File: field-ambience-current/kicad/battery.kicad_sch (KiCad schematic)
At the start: 16 parts, among them J9 JST PH 2.0 2-pin (LiPo Batter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, Q1 DMG2305UX P-MOS SOT-23 (USB-C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, U7 MCP73831T-2ACI/OT (LiPo Charg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, U8 TPS61089RNSR (Boost LiPo→5V, 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

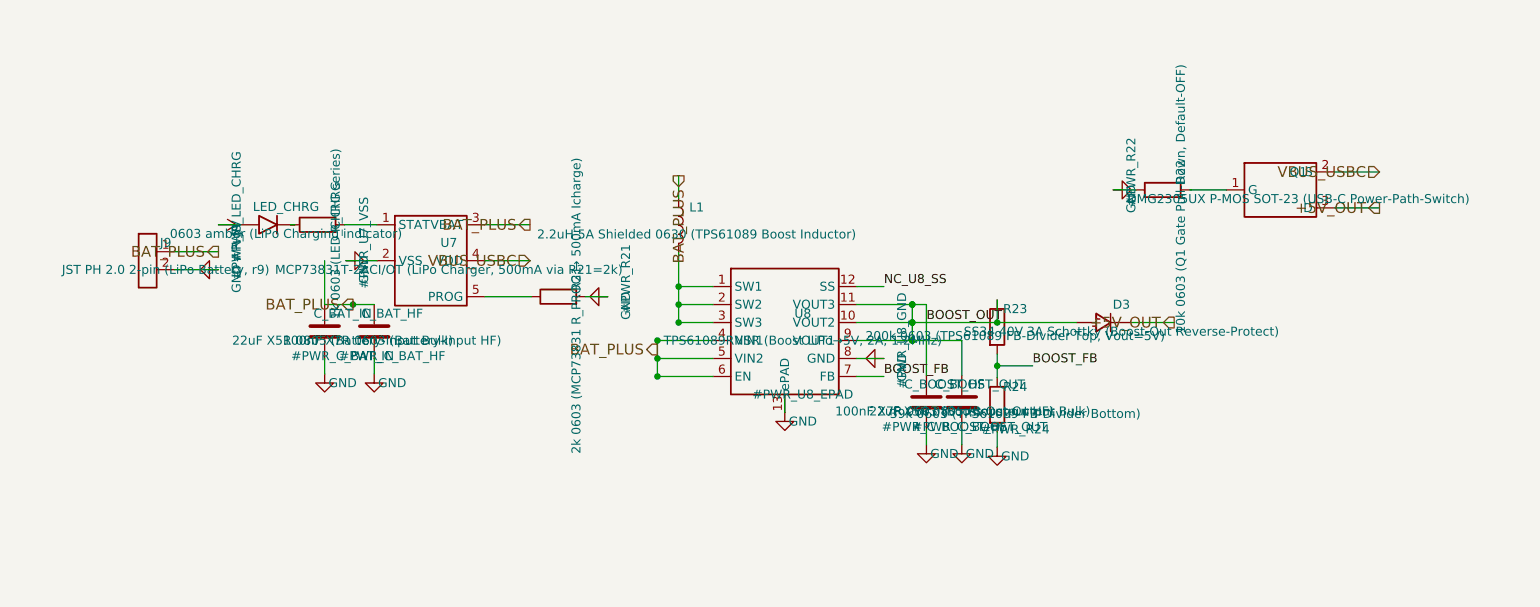
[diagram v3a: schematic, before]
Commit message: pcb(gen): r12-B11 RESOLVED — TPS61089-Refactor RNSR → RNR (JLC-soviel-wie-möglich)
User-Decision: Option 1 (JLC-Bestücken-Strategie). TPS61089RNSR (QFN-12 3×3
nicht bei LCSC verfügbar) gegen TPS61089RNR (VQFN-11 HotRod 2×2.5 + ePAD,
LCSC C165129 Extended $0.41, 2.775 Stock) getauscht.

Generator-Changes:
- _tps61089_lib_symbol() komplett neu auf 11 Pins per TI Datasheet SLVSD38C:
  FSW, VCC, FB, COMP, GND, VOUT (left); SW, BOOT, VIN, ILIM, EN (right); ePAD
- battery_sheet U8-Block komplett umverdrahtet — neuer Pinout, alle 11 Pins
  + ePAD korrekt connected
- 6 neue externe Bauteile (alle BASIC oder PREFERRED, keine Extended-Fees!):
  * C_VCC 1µF (C15849) — interne LDO-Decoupling (Datasheet >=1µF)
  * R_FSW 360k (C23146 PREF) — Fsw ~1.21 MHz (über Audio-Band wie SPEC)
  * R_ILIM 20k (C4184) — current-limit ~4A peak (matches TPS-2A-output)
  * C_BOOT 100nF (C14663) — high-side gate-driver bootstrap zwischen BOOT+SW
  * R_COMP 22k (C31850) + C_COMP 1nF (C1588) — Type-II loop-compensation

Side-Bug aufgefangen während Refactor: erste R23-pin1-Wire ging vertikal
DURCH R23+R24-Body und shortete den FB-Divider (Analyzer zeigte BOOST_FB 6 pins
statt 3 inkl. U8.6 VOUT). Fix: Label-only-Connect statt durchgehende Wire.

Analyzer-Result nach Refactor (verifiziert via kicad-skill):
- Errors: 6 (unchanged, alle pre-existing VM-001 false-positives)
- Warnings: 22 → 21
- Trust: 79.8% → 81.4%
- Critical Nets korrekt connected:
  * BAT_PLUS: 8 pins (R_BAT_DIV_TOP, J9.1, U7.3, C_BAT_IN/HF, U8.9 VIN,
    U8.7 EN, L1.1)
  * BOOST_OUT: 5 pins (U8.6 VOUT, R23.1, C_BOOST_OUT, C_BOOST_HF, D3.2 A)
  * BOOST_FB: 3 pins (U8.3 FB, R23.2, R24.1) — Divider sauber
  * U8_SW_NODE: 4 pins (U8.11 SW, L1.2, C_BOOT.2, R_FSW.1)
  * U8_BOOT_NODE: 2 pins (U8.10 BOOT, C_BOOT.1)

SPEC §2.2 + PCB_TODO r12-B11 als RESOLVED markiert. Footprint
"Package_DFN_QFN:VQFN-11-1EP_2.6x2.6mm_P0.5mm_EP0.85x1.5mm_HotRod" als String
gesetzt — die exakte KiCad-Library-Match muss im KiCad-GUI verifiziert werden
(könnte ein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
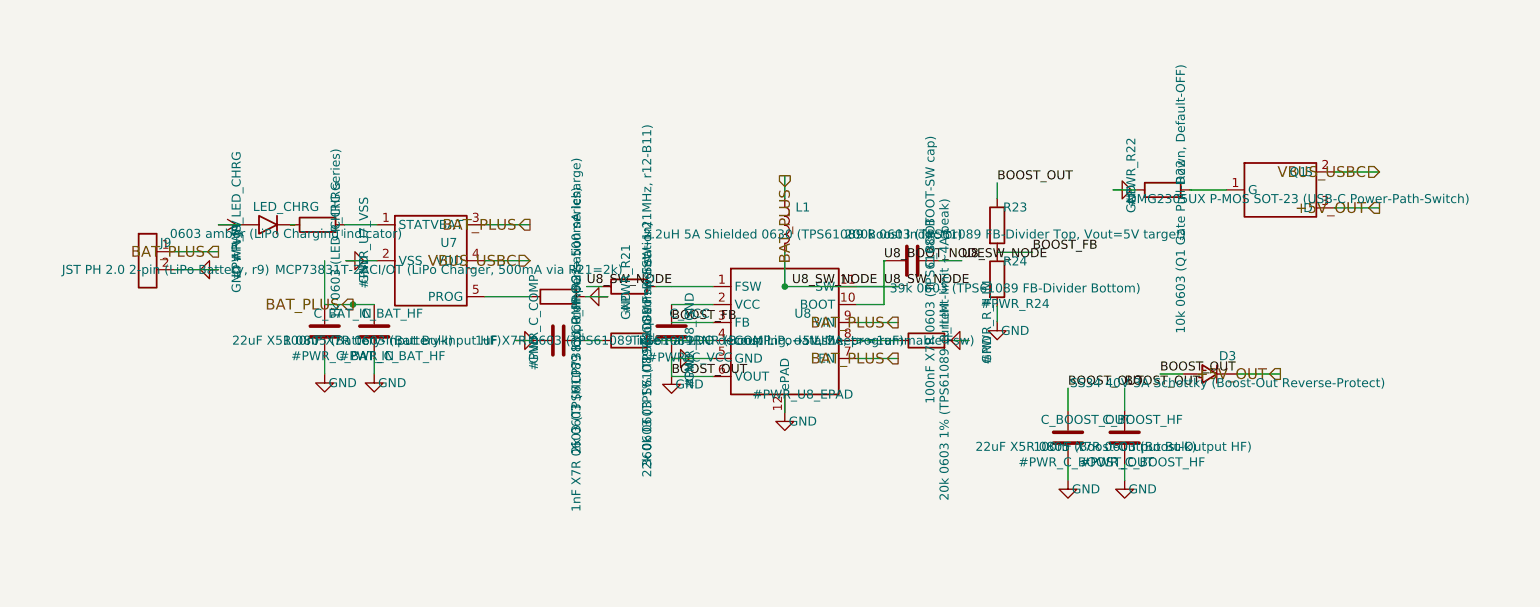
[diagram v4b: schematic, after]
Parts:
- added C_BOOT: 100nF X7R 0603 (TPS61089 BOOT-SW cap), Capacitor_SMD:C_0603_1608Metric, symbol Device:C
- added C_COMP: 1nF X7R 0603 (TPS61089 loop-compensation series), Capacitor_SMD:C_0603_1608Metric, symbol Device:C
- added C_VCC: 1uF X7R 0603 (TPS61089 internal LDO decoupling, d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, Capacitor_SMD:C_0603_1608Metric, symbol Device:C
- added R_COMP: 22k 0603 (TPS61089 loop-compensation), Resistor_SMD:R_0603_1608Metric, symbol Device:R
- added R_FSW: 360k 0603 1% (TPS61089 Fsw-Set ~1.21MHz, r12-B11), Resistor_SMD:R_0603_1608Metric, symbol Device:R
- added R_ILIM: 20k 0603 1% (TPS61089 current-limit ~4A peak), Resistor_SMD:R_0603_1608Metric, symbol Device:R
- R23: value 200k 0603 (TPS61089 FB-Divider Top, Vout=5V) -> 200k 0603 (TPS61089 FB-Divider Top, Vout=5V target)
- U8: value TPS61089RNSR (Boost LiPo→5V, 2A, 1.2MHz) -> TPS61089RNR (Boost LiPo→5V, 2A, programmable Fsw); footprint Package_DFN_QFN:VQFN-12-1EP_3x3mm_P0.5mm_EP1.5x1.5mm -> Package_DFN_QFN:VQFN-11-1EP_2.6x2.6mm_P0.5mm_EP0.85x1.5mm_HotRod; LCSC TBD-USER-SUPPLY-or-RNRR-refactor -> C165129; MPN TPS61089RNSR -> TPS61089RNR
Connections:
- net NC_U8_SS is gone; now on net GND: U8.12 (ePAD)
- net BAT_PLUS: now also U8.7 (EN), U8.9 (VIN); no longer U8.4 (VIN1), U8.5 (VIN2), U8.6 (EN)
- net BOOST_FB: now also U8.3 (FB); no longer U8.7 (FB)
- net BOOST_OUT: now also U8.6 (VOUT); no longer U8.10 (VOUT2), U8.11 (VOUT3), U8.9 (VOUT1)
- net GND: now also U8.5 (GND), C_COMP.1, C_VCC.2, R_ILIM.2; no longer U8.13 (ePAD), U8.8 (GND)
- new net: C_COMP.2, R_COMP.1
- new net: R_COMP.2, U8.4 (COMP)
- new net: R_FSW.2, U8.1 (FSW)
- new net: C_VCC.1, U8.2 (VCC)
- new net: R_ILIM.1, U8.8 (ILIM)
- new net U8_BOOT_NODE: C_BOOT.1, C_BOOT.2, L1.2, R_FSW.1, U8.10 (BOOT), U8.11 (SW)
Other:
- moved on the sheet: C_BOOST_HF, C_BOOST_OUT, D3, L1, R23, R24
